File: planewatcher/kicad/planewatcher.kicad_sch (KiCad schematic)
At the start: 9 parts, among them J1 Conn_01x02, J2 RF_IN, J3 BMI-S-209-F, J4 FPGA BANK 33, J5 FPGA BANK 35 V1.2/V1.3

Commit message: updates before fab
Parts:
- FL1, FL2: Purpose (none) -> Band-limits the ADS-B 1090MHz RF path and rejects out-of-ba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; Suggested Part (none) -> Tai-Saw TA2003A
- J1: Purpose (none) -> Provides the external DC power input connection.; Suggested Part (none) -> Phoenix Contact 1729128
- J2: Purpose Accepts the external 1090 MHz antenna input -> Accepts the external 1090MHz antenna input.; Suggested Part (none) -> Amphenol RF 132289
- J3: Purpose (none) -> Shields the RF front-end area from external and board-level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; Suggested Part (none) -> Laird/BMI BMI-S-209-F
- J4: Purpose (none) -> Breaks out FPGA bank 33 I/O and power pins to the carrier/F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; Suggested Part (none) -> Samtec TSW-120-07-L-D
- J5: Purpose (none) -> Breaks out FPGA bank 35 I/O and power pins to the carrier/F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; Suggested Part (none) -> Samtec TSW-120-07-L-D
- JP2: Purpose (none) -> Selects the prototype RF-stage supply rail.; Suggested Part (none) -> Samtec TSW-103-07-L-S
- JP3: Purpose (none) -> Selects the prototype ADC digital supply rail.; Suggested Part (none) -> Samtec TSW-103-07-L-S

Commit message: updates before fab
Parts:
- J1, J2, J4, J5: now not fitted
- JP2, JP3: now not fitted; now in the parts list
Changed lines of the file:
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@@
 	(polyline
 		(pts
-			(xy 200.928 173.185) (xy 200.928 173.185)
-		)
-		(stroke
-			(width -0.0001)
-			(type solid)
-		)
-		(fill
-			(type color)
-			(color 211 209 209 1)
-		)
-	)
-	(polyline
-		(pts
 			(xy 217.4894 172.2182) (xy 217.5914 172.2262) (xy 217.6893 172.2395) (xy 217.7833 172.258) (xy 217.8734 172.2817)
 			(xy 217.9596 172.3105) (xy 218.042 172.3444) (xy 218.1206 172.3834) (xy 218.1954 172.4273) (xy 218.2666 172.4762)
@@
 		)
 	)
+	(polyline
+		(pts
+			(xy 200.928 173.185) (xy 200.928 173.185)
+		)
+		(stroke
+			(width -0.0001)
+			(type solid)
+		)
+	)
 	(wire
 		(pts
@@
 		(on_board yes)
 		(in_pos_files yes)
-		(dnp no)
+		(dnp yes)
 		(fields_autoplaced yes)
 		(property "Reference" "J5"
@@
 		(on_board yes)
 		(in_pos_files yes)
-		(dnp no)
+		(dnp yes)
 		(property "Reference" "J1"
 			(at 21.59 41.91 0)
@@
 		(body_style 1)
 		(exclude_from_sim no)
-		(in_bom no)
+		(in_bom yes)
 		(on_board yes)
 		(in_pos_files yes)
-		(dnp no)
+		(dnp yes)
 		(fields_autoplaced yes)
 		(property "Reference" "JP3"
@@
 		(on_board yes)
 		(in_pos_files yes)
-		(dnp no)
+		(dnp yes)
 		(fields_autoplaced yes)
 		(property "Reference" "J4"
@@
 		(body_style 1)
 		(exclude_from_sim no)
-		(in_bom no)
+		(in_bom yes)
 		(on_board yes)
 		(in_pos_files yes)
-		(dnp no)
+		(dnp yes)
 		(fields_autoplaced yes)
 		(property "Reference" "JP2"
@@
 		(on_board yes)
 		(in_pos_files yes)
-		(dnp no)
+		(dnp yes)
 		(property "Reference" "J2"
 			(at 22.1096 86.36 0)

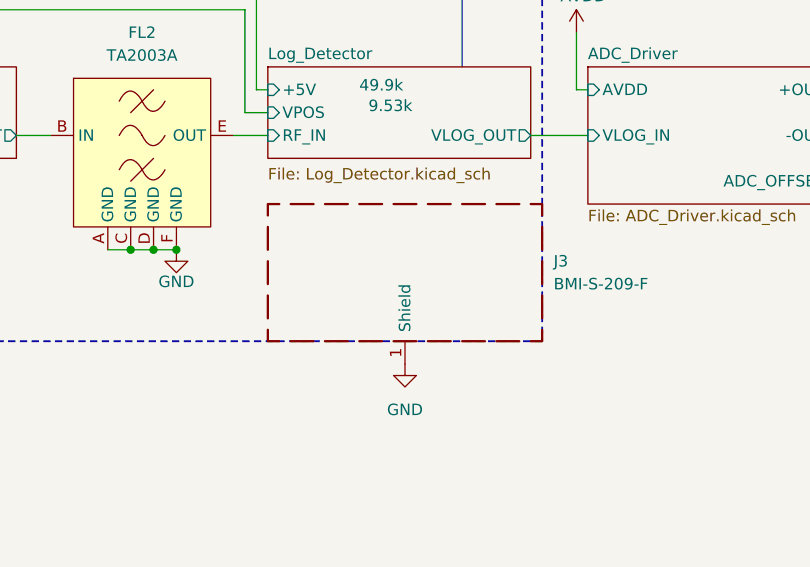
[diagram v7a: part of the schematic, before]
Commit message: mark RF shield as do not populate for prototype
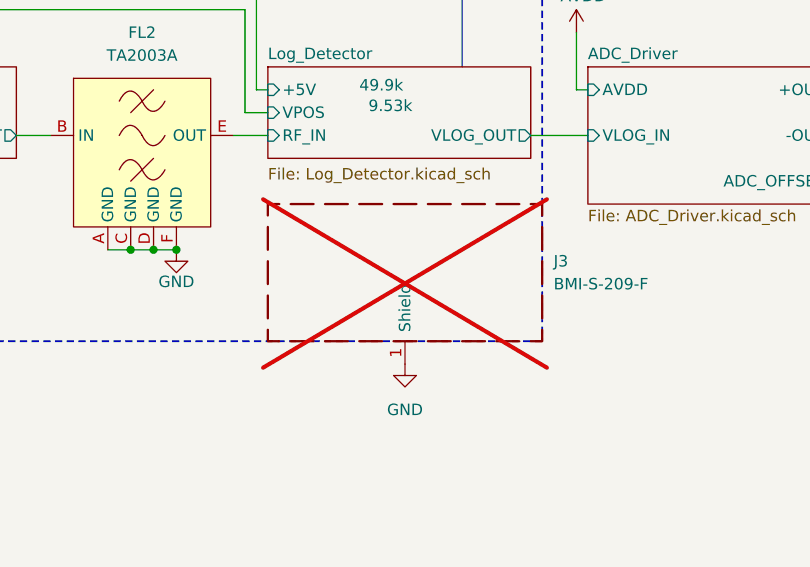
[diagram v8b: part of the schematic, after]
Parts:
- J3: now not fitted
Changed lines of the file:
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@@
 		(on_board yes)
 		(in_pos_files yes)
-		(dnp no)
+		(dnp yes)
 		(fields_autoplaced yes)
 		(property "Reference" "J3"
